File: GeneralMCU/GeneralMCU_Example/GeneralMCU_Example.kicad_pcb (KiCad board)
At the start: 2 copper layers, 1 part, among them U1 SMD42

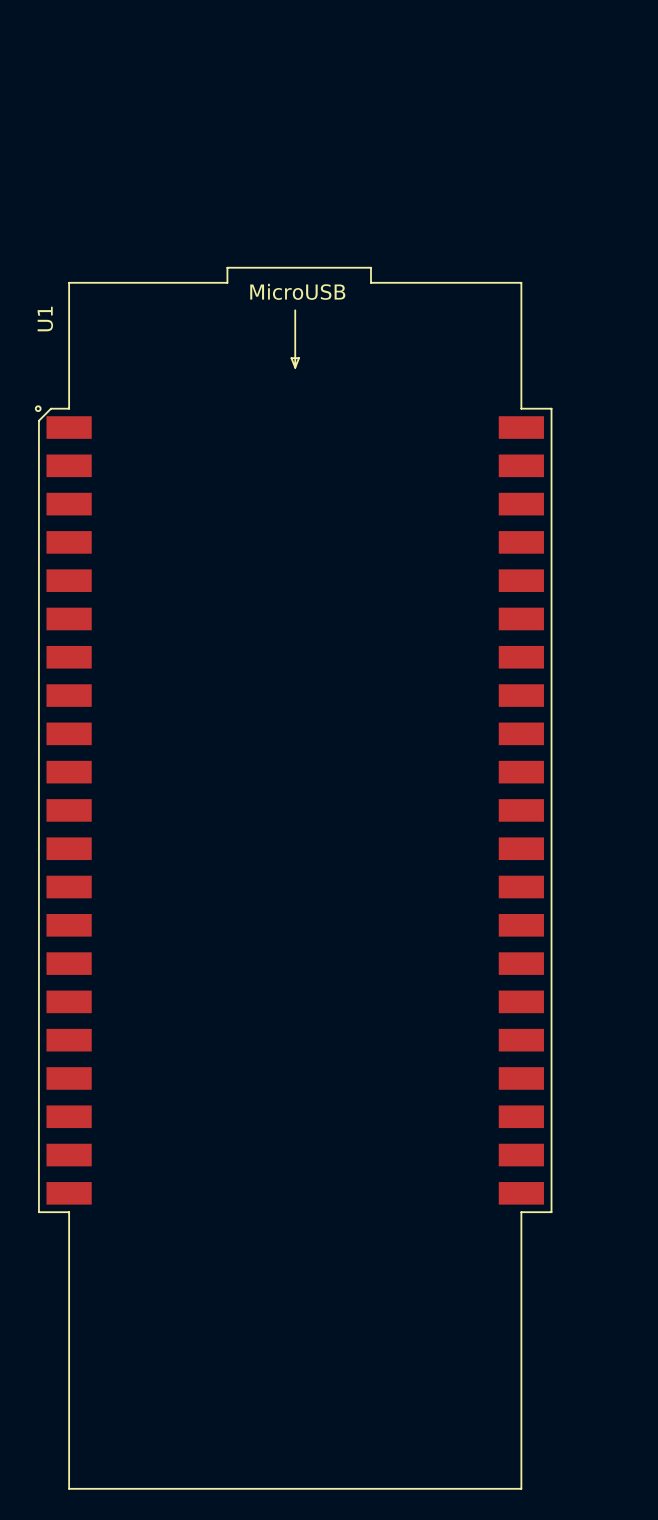
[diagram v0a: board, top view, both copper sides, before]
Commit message: Updated Example project and smd sym and footprint for recieving pcbs.
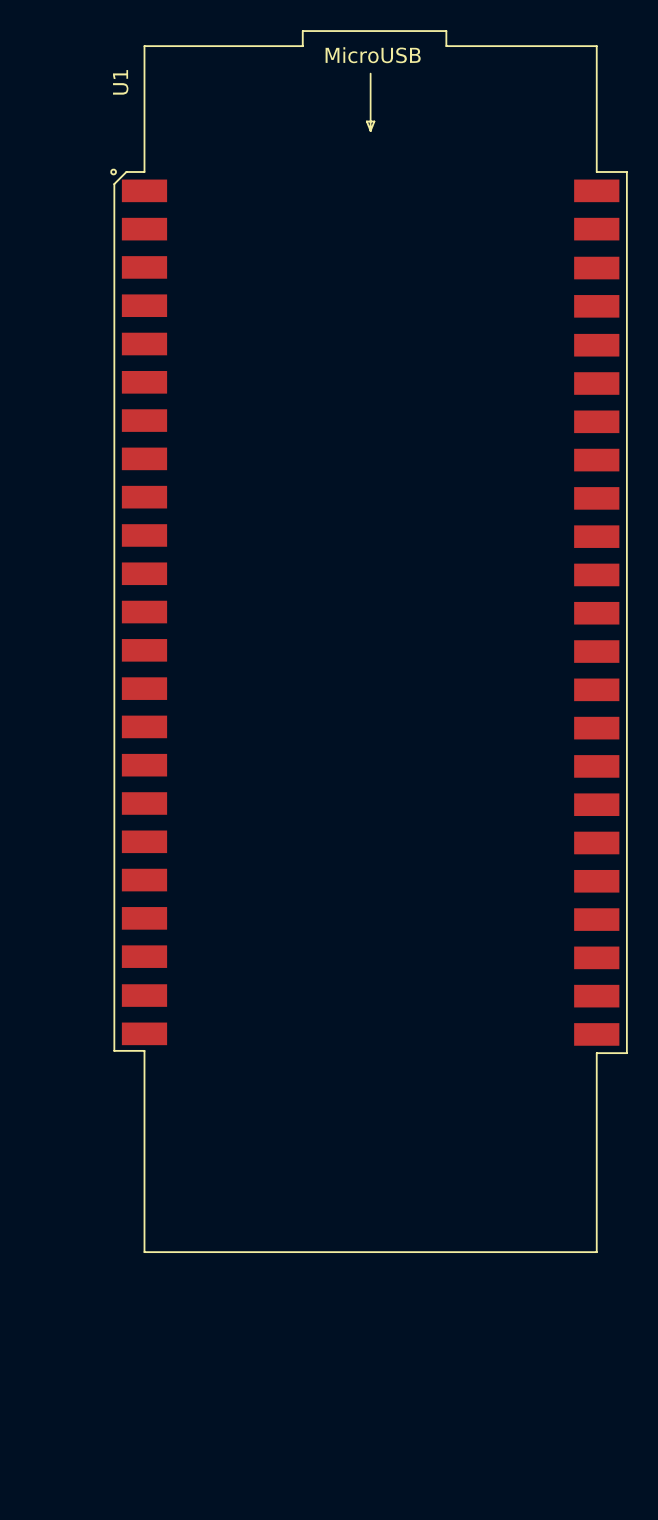
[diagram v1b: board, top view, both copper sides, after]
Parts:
- U1: value SMD42 -> SMD46
- moved U1 16.5 mm to (149.1, 78.9)
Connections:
- U1 pad 22: +V -> GND
- U1 pad 23: /PA10 -> Net-(U1-Pad23)
- U1 pad 24: /PA9 -> Net-(U1-Pad24)
- U1 pad 25: /PA8 -> GND
- U1 pad 26: /PC9 -> +V
- U1 pad 27: /PC8 -> /PA10
- U1 pad 28: /PC7 -> /PA9
- U1 pad 29: /PC6 -> /PA8
- U1 pad 30: /PB15 -> /PC9
- U1 pad 31: /PC10 -> /PC8
- U1 pad 32: /PC11 -> /PC7
- U1 pad 33: /PC12 -> /PC6
- U1 pad 34: /I2C1_SCL -> /PB15
- U1 pad 35: /I2C1_SDA -> /PC10
- U1 pad 36: /PC0 -> /PC11
- U1 pad 37: /PC1 -> /PC12
- U1 pad 38: /PC2 -> /I2C1_SCL
- U1 pad 39: /PC3 -> /I2C1_SDA
- U1 pad 40: /PA0 -> /PC0
- U1 pad 41: /PA1 -> /PC1
- U1 pad 42: /PA2 -> /PC2
